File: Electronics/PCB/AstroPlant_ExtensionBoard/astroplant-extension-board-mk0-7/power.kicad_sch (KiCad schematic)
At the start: 10 parts, among them J20 Conn_01x02, J21 Conn_01x02

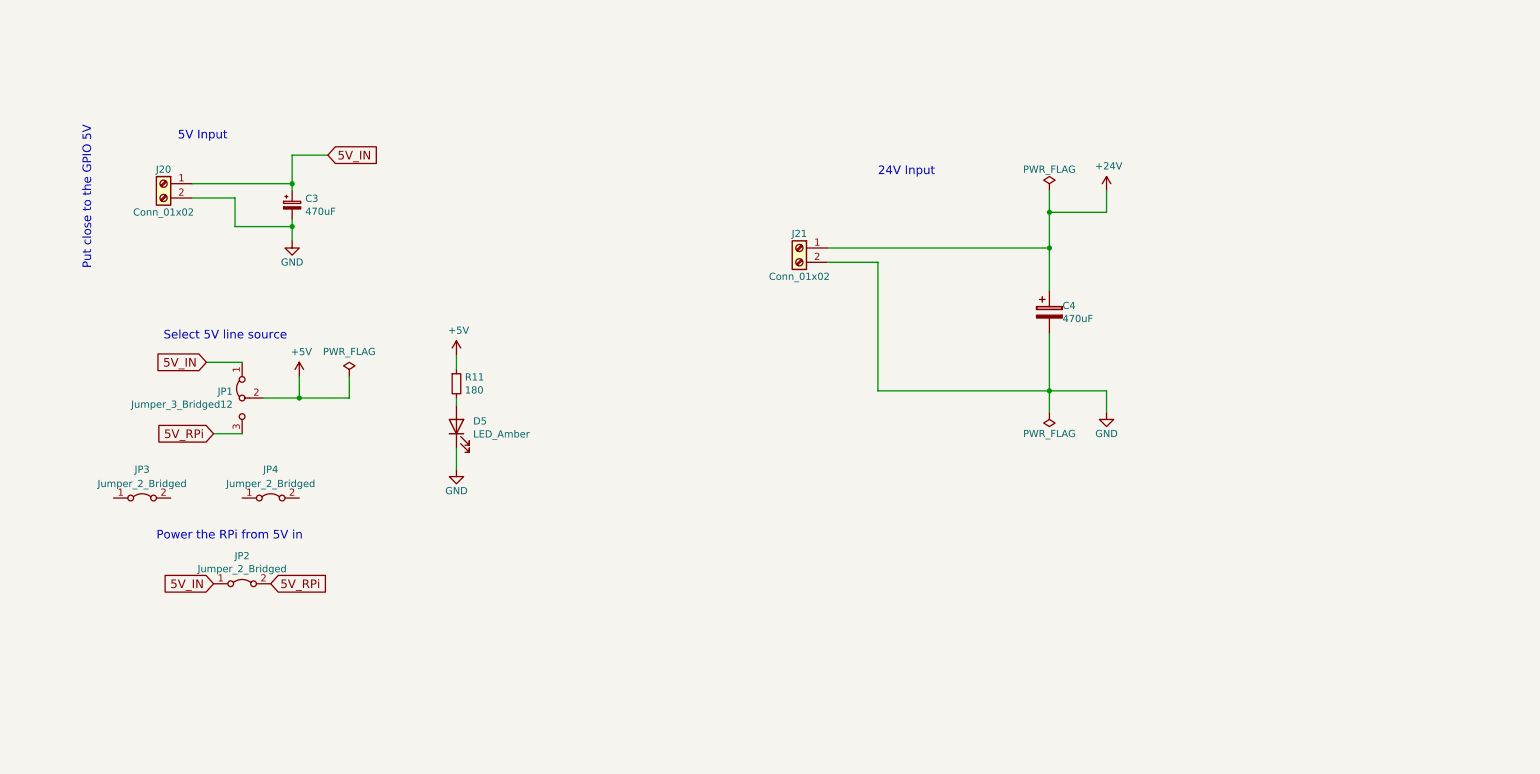
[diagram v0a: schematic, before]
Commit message: Update schematic and change library path
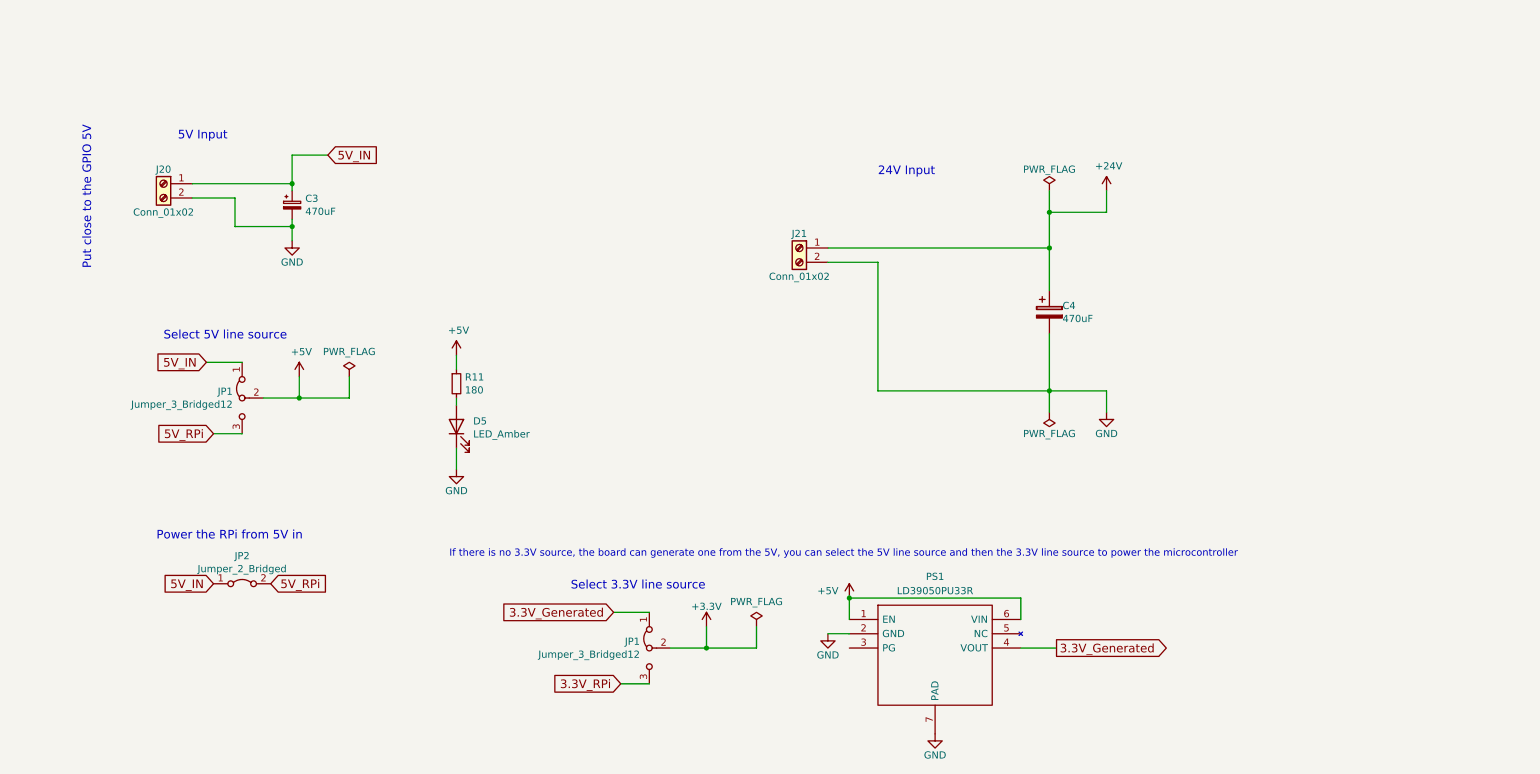
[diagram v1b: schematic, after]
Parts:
- removed JP3, JP4: Jumper_2_Bridged, symbol Jumper:Jumper_2_Bridged
- added JP1: Jumper_3_Bridged12, Connector_PinHeader_2.54mm:PinHeader_1x03_P2.54mm_Vertical, symbol Astroplant_VFR-rescue:Jumper_3_Bridged12-Jumper
- added PS1: LD39050PU33R, SamacSys_Parts:SON95P300X300X100-7N-D, symbol SamacSys_Parts:LD39050PU33R
- J20, J21: footprint footprints:TerminalBlock_bornier-2_P5.08mm -> SamacSys_Parts:SHDR2W100P0X500_1X2_1000X750X990P
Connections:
- net +5V: now also PS1.1 (EN), PS1.6 (VIN)
- net GND: now also PS1.2 (GND), PS1.7 (PAD)
- new net +3V3: JP1.2 (C)
- new net 3.3V_Generated: JP1.1 (A), PS1.4 (VOUT)
- new net 3.3V_RPi: JP1.3 (B)
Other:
- note added: "If there is no 3.3V source, the board can generate one from the 5V, you can select the 5V line source and then the 3.3V line source to power the microcontroller"
- note added: "Select 3.3V line source"

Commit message: Place components on PCB
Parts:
- removed R11: 180, Resistor_SMD:R_0805_2012Metric, symbol Device:R_Small
- added R12: 180, Resistor_SMD:R_0603_1608Metric, symbol Device:R_Small
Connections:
- net +5V: now also R12.2
- net at D5.2 (A): now also R12.1
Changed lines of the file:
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@@
-    )
-  )
-  (symbol (lib_id "Device:R_Small") (at 118.11 97.79 0) (unit 1)
-    (in_bom yes) (on_board yes) (dnp no)
-    (property "Reference" "R11" (at 119.6086 96.6216 0)
-      (effects (font (size 1.27 1.27)) (justify left))
-    )
-    (property "Value" "180" (at 119.6086 98.933 0)
-      (effects (font (size 1.27 1.27)) (justify left))
-    )
-    (property "Footprint" "Resistor_SMD:R_0805_2012Metric" (at 118.11 97.79 0)
-      (effects (font (size 1.27 1.27)) hide)
-    )
-    (property "Datasheet" "http://www.rohm.com/web/global/datasheet/ESR01MZPF/esr-e" (at 118.11 97.79 0)
-      (effects (font (size 1.27 1.27)) hide)
-    )
-    (property "MPN" "ESR10EZPJ181" (at 118.11 97.79 0)
-      (effects (font (size 1.27 1.27)) hide)
-    )
-    (property "Digikey PN" "RHM180KCT-ND" (at 118.11 97.79 0)
-      (effects (font (size 1.27 1.27)) hide)
-    )
-    (pin "1")
-    (pin "2")
-    (instances
-      (project "Astroplant_VFR"
-        (path "/4e818498-015c-45b7-982b-80c19490efdc/00000000-0000-0000-0000-00005a8053d4"
-          (reference "R11") (unit 1)
-        )
-      )
-      (project "Astroplant_AL"
-        (path "/51acab52-3cd6-4bba-9dee-c12efd332038/00000000-0000-0000-0000-00005a8053d4"
-          (reference "R11") (unit 1)
-        )
-      )
     )
   )
@@
         )
       )
+    )
+  )
+  (symbol (lib_id "Device:R_Small") (at 118.11 97.79 180) (unit 1)
+    (in_bom yes) (on_board yes) (dnp no) (fields_autoplaced)
+    (property "Reference" "R12" (at 120.65 96.52 0)
+      (effects (font (size 1.27 1.27)) (justify right))
+    )
+    (property "Value" "180" (at 120.65 99.06 0)
+      (effects (font (size 1.27 1.27)) (justify right))
+    )
+    (property "Footprint" "Resistor_SMD:R_0603_1608Metric" (at 118.11 97.79 0)
+      (effects (font (size 1.27 1.27)) hide)
+    )
+    (property "Datasheet" "~" (at 118.11 97.79 0)
+      (effects (font (size 1.27 1.27)) hide)
+    )
+    (property "MPN" "CRCW0603180RFKEA" (at 118.11 97.79 0)
+      (effects (font (size 1.27 1.27)) hide)
+    )
+    (pin "1")
+    (pin "2")
+    (instances
+      (project "Astroplant_AL"
+        (path "/51acab52-3cd6-4bba-9dee-c12efd332038/5f0c961f-7fa6-4a15-8a74-755a432cc19e"
+          (reference "R12") (unit 1)
+        )
+        (path "/51acab52-3cd6-4bba-9dee-c12efd332038/00000000-0000-0000-0000-00005a8053d4"
+          (reference "R11") (unit 1)
+        )
+      )

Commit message: Completed version of the project
Generate outputs (BOM, Drill, Pkp, Gerber)
Added connectors descritption (like "I2C 3.3V" dor the corresponding connector)
Added a connector to an external antenna
Changed routing
Changed component placement
Added a script to generate a usable BOM
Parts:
- removed C4: 470uF, Capacitor_SMD:CP_Elec_10x10.5, symbol Astroplant_VFR-rescue:CP-Device
- removed JP1: Jumper_3_Bridged12, Connector_PinHeader_2.54mm:PinHeader_1x03_P2.54mm_Vertical, symbol Astroplant_VFR-rescue:Jumper_3_Bridged12-Jumper
- removed JP2: Jumper_2_Bridged, Connector_PinHeader_2.54mm:PinHeader_1x02_P2.54mm_Vertical, symbol Jumper:Jumper_2_Bridged
- added C15, C16: 1uF 16VDC, CAPC1608X50N, symbol SamacSys_Parts:GRM185R61C105KE44D
- added C4: 875115652007, CAPAE830X900N, symbol SamacSys_Parts:875115652007
- added C9 (x3): 100nF, Capacitor_SMD:C_0603_1608Metric, symbol Device:C_Small
- added J14: 61300621121, HDRV6W64P254_2X3_762X508X889P, symbol SamacSys_Parts:61300621121
- PS1: MPN (none) -> LD39050PU33R
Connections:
- net +24V: now also C4.1
- net +5V: now also C15.1, C9.1, J14.1, J14.3, J14.5
- net 3.3V_Generated: now also C16.1, C9.1
- net 5V_IN: now also J14.4
- net 5V_RPi: now also J14.2
- net GND: now also C15.2, C16.2, C4.2, C9.2, C9.2
- new net 5V_USB: J14.6
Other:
- note removed: "Power the RPi from 5V in"

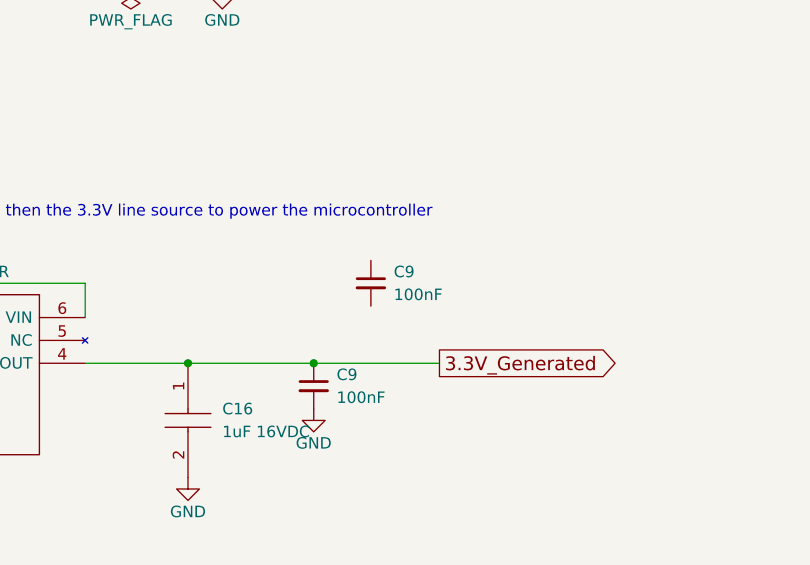
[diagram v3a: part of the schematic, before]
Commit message: Solved processing notes from aisler by changing micro usb connector
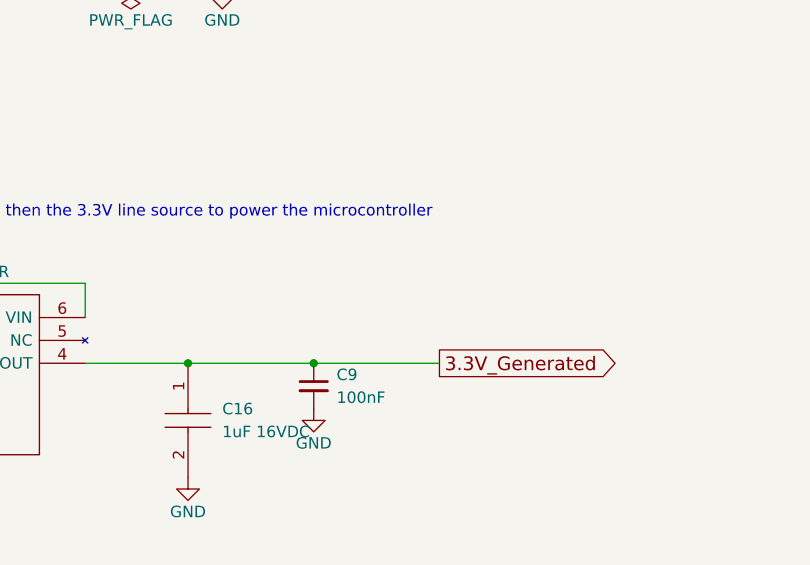
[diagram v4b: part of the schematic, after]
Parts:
- removed C9: 100nF, Capacitor_SMD:C_0603_1608Metric, symbol Device:C_Small
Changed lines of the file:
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@@
-    )
-  )
-  (symbol (lib_id "Device:C_Small") (at 250.19 135.89 0) (unit 1)
-    (in_bom yes) (on_board yes) (dnp no) (fields_autoplaced)
-    (property "Reference" "C9" (at 252.73 134.6263 0)
-      (effects (font (size 1.27 1.27)) (justify left))
-    )
-    (property "Value" "100nF" (at 252.73 137.1663 0)
-      (effects (font (size 1.27 1.27)) (justify left))
-    )
-    (property "Footprint" "Capacitor_SMD:C_0603_1608Metric" (at 250.19 135.89 0)
-      (effects (font (size 1.27 1.27)) hide)
-    )
-    (property "Datasheet" "~" (at 250.19 135.89 0)
-      (effects (font (size 1.27 1.27)) hide)
-    )
-    (property "MPN" "VJ0603Y104MXJCW1BC" (at 250.19 135.89 0)
-      (effects (font (size 1.27 1.27)) hide)
-    )
-    (pin "1")
-    (pin "2")
-    (instances
-      (project "Astroplant_AL"
-        (path "/51acab52-3cd6-4bba-9dee-c12efd332038/5f0c961f-7fa6-4a15-8a74-755a432cc19e"
-          (reference "C9") (unit 1)
-        )
-        (path "/51acab52-3cd6-4bba-9dee-c12efd332038"
-          (reference "C1") (unit 1)
-        )
-        (path "/51acab52-3cd6-4bba-9dee-c12efd332038/00000000-0000-0000-0000-00005a8053d4"
-          (reference "C22") (unit 1)
-        )
-      )
     )
   )
